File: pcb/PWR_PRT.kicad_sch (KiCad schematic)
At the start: 2 parts, among them U5 TA6F27CA

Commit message: added USB protection, reviewed LSD and HSD, improved input TVS footprint
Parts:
- U5: footprint Diode_SMD:Vishay_SMPA -> Diode_SMD:D_SOD-128
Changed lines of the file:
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@@
 			)
 		)
-		(property "Footprint" "Diode_SMD:Vishay_SMPA"
+		(property "Footprint" "Diode_SMD:D_SOD-128"
 			(at 118.11 62.2299 90)
 			(effects

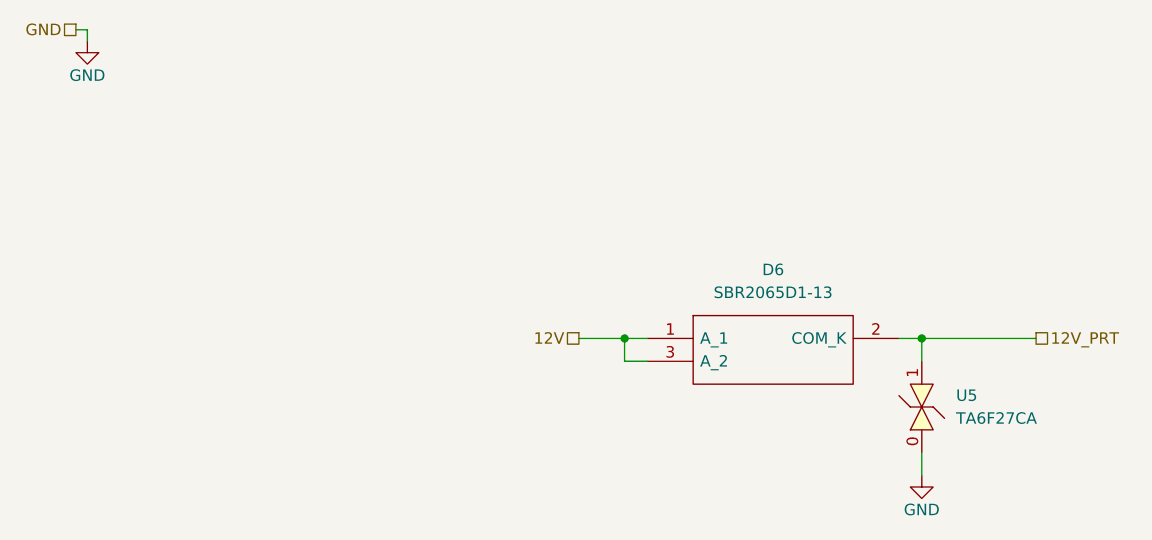
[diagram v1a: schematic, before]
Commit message: reannotated, updated some symbols
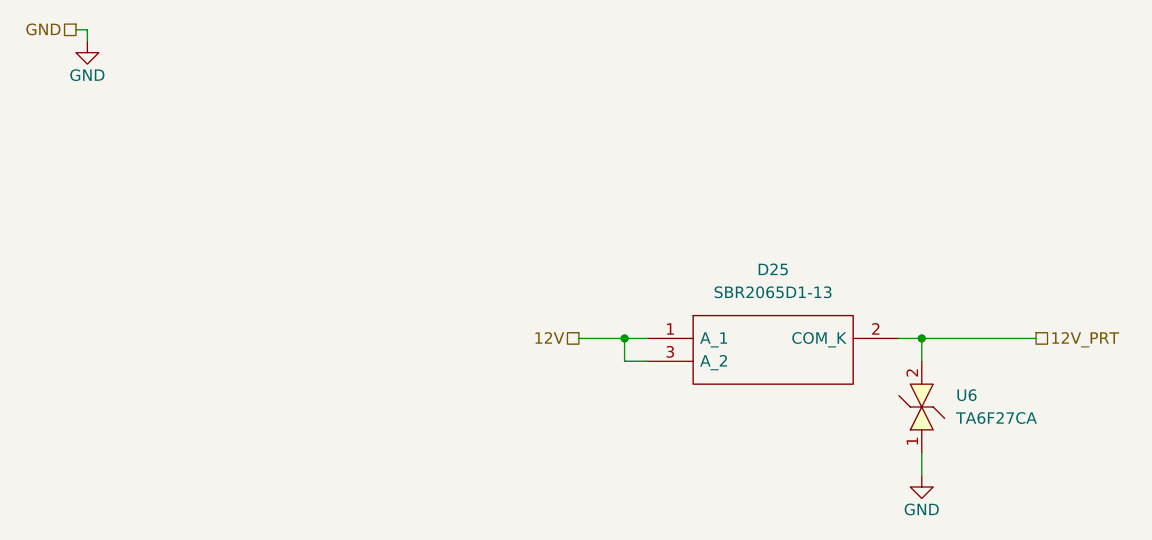
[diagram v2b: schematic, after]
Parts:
- renumbered D6 to D25, U5 to U6
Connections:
- net 12V_PRT: now also U6.2; no longer U6.1
- net GND: now also U6.1; no longer U6.0
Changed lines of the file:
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@@
 		(dnp no)
 		(fields_autoplaced yes)
-		(property "Reference" "D6"
+		(property "Reference" "D25"
 			(at 97.79 44.45 0)
 			(effects
@@
 			(project ""
 				(path "/3aee14c3-5480-4f7c-989e-3fef81779034/05e3be97-98f6-4518-a1a7-240d4da327e6/8dbaa3b5-05a2-4c92-8247-baeb1ffbc2d0"
-					(reference "D6")
+					(reference "D25")
 					(unit 1)
 				)
@@
 		(on_board yes)
 		(dnp no)
-		(property "Reference" "#PWR0340"
+		(property "Reference" "#PWR0407"
 			(at 114.3 73.66 0)
 			(effects
@@
 			(project "NCU"
 				(path "/3aee14c3-5480-4f7c-989e-3fef81779034/05e3be97-98f6-4518-a1a7-240d4da327e6/8dbaa3b5-05a2-4c92-8247-baeb1ffbc2d0"
-					(reference "#PWR0340")
+					(reference "#PWR0407")
 					(unit 1)
 				)
@@
 		(on_board yes)
 		(dnp no)
-		(property "Reference" "#PWR0339"
+		(property "Reference" "#PWR0406"
 			(at 21.59 25.4 0)
 			(effects
@@
 			(project "NCU"
 				(path "/3aee14c3-5480-4f7c-989e-3fef81779034/05e3be97-98f6-4518-a1a7-240d4da327e6/8dbaa3b5-05a2-4c92-8247-baeb1ffbc2d0"
-					(reference "#PWR0339")
+					(reference "#PWR0406")
 					(unit 1)
 				)
@@
 		(dnp no)
 		(fields_autoplaced yes)
-		(property "Reference" "U5"
+		(property "Reference" "U6"
 			(at 118.11 58.4199 90)
 			(effects
@@
 			)
 		)
-		(pin "0"
+		(pin "2"
 		)
 		(pin "1"
@@
 			(project ""
 				(path "/3aee14c3-5480-4f7c-989e-3fef81779034/05e3be97-98f6-4518-a1a7-240d4da327e6/8dbaa3b5-05a2-4c92-8247-baeb1ffbc2d0"
-					(reference "U5")
+					(reference "U6")
 					(unit 1)
 				)
